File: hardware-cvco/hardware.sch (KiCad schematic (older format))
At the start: 2 parts, among them J1 Conn_Coaxial, Y1 CVCO55

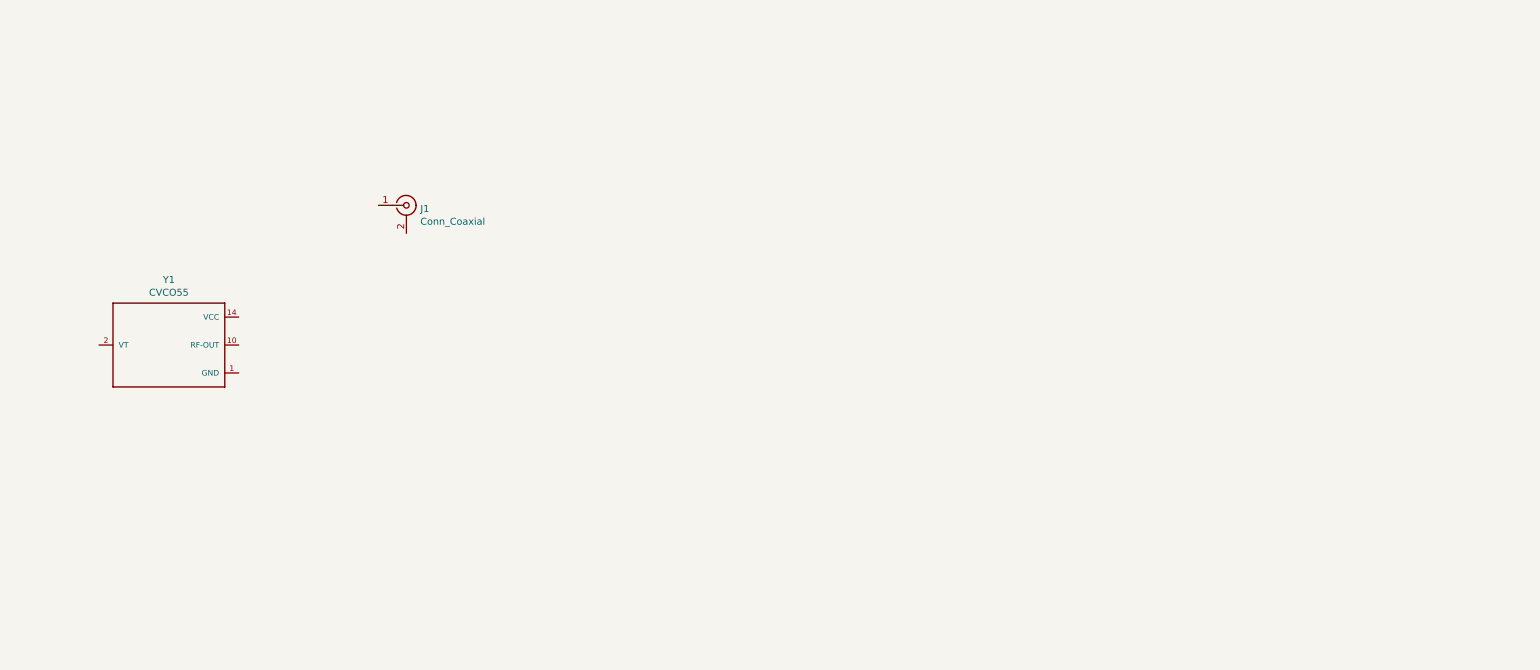
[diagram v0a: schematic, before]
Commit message: 500-1000 MHz & 1000-2000 MHz Crystek VCOs.
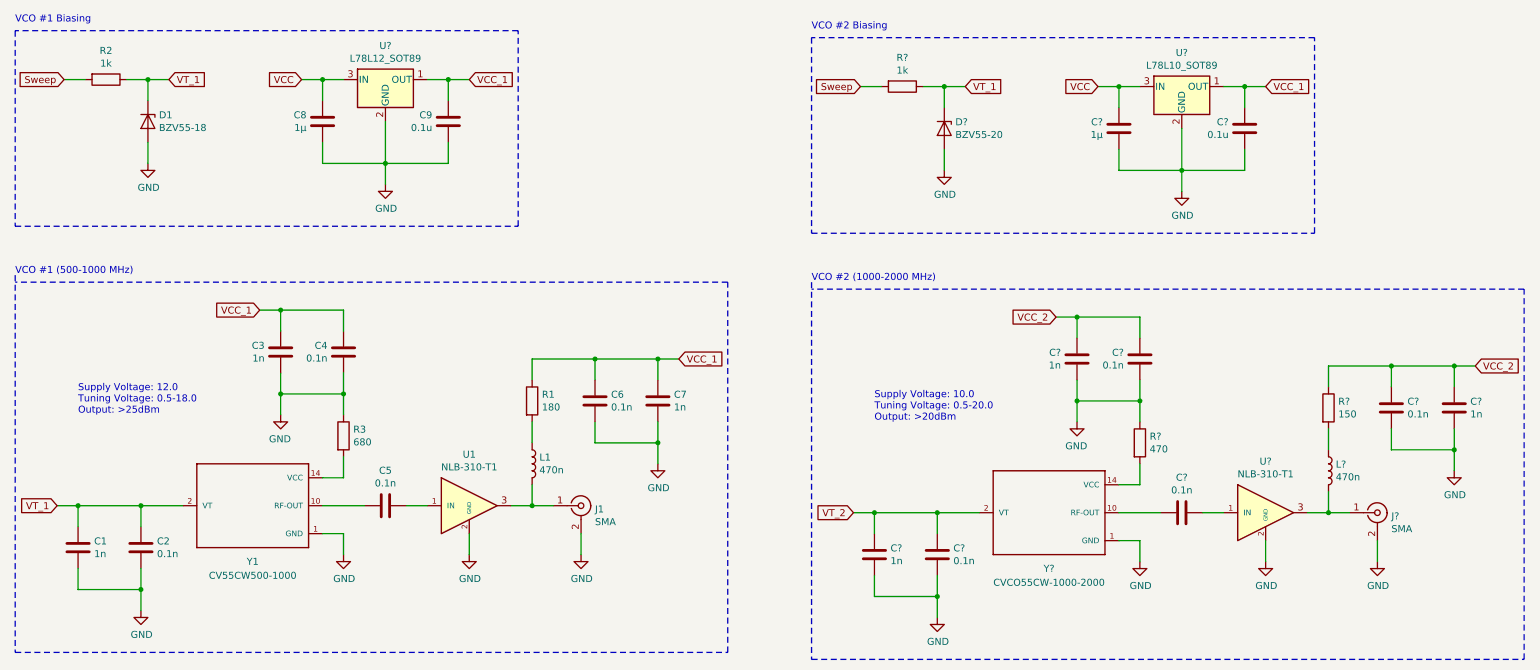
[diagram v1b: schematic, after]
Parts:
- added C1, C3, C7, C? (x3): 1n, symbol Device:C
- added C2, C4, C5, C6, C? (x4): 0.1n, symbol Device:C
- added C8, C?: 1μ, symbol Device:C
- added C9, C?: 0.1u, symbol Device:C
- added D1: BZV55-18, symbol Device:D_Zener
- added D?: BZV55-20, symbol Device:D_Zener
- added J?: SMA, Connector_Coaxial:SMA_Amphenol_132134_Vertical, symbol Connector:Conn_Coaxial
- added L1, L?: 470n, symbol Device:L
- added R1: 180, symbol Device:R
- added R2, R?: 1k, symbol Device:R
- added R3: 680, symbol Device:R
- added R?: 150, symbol Device:R
- added R?: 470, symbol Device:R
- added U1, U?: NLB-310-T1, CVCO:Micro-X-4, symbol CVCO:NLB-310
- added U?: L78L12_SOT89, Package_TO_SOT_SMD:SOT-89-3, symbol Regulator_Linear:L78L12_SOT89
- added U?: L78L10_SOT89, Package_TO_SOT_SMD:SOT-89-3, symbol Regulator_Linear:L78L10_SOT89
- added Y?: CVCO55CW-1000-2000, CVCO:CVCO55, symbol CVCO:CVCO55
- J1: value Conn_Coaxial -> SMA
- Y1: value CVCO55 -> CV55CW500-1000
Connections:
- net GND: now also J1.2 (Ext), C1.2, C2.2, C3.2, C4.2, C6.2, C7.2, C8.2, C9.2, C?.2, C?.2, C?.2, C?.2, C?.2, C?.2, C?.2, C?.2, D1.2 (A), D?.2 (A), J?.2 (Ext), R3.1, R?.1, U1.2 (GND), U1.4 (GND), U?.2 (GND), U?.2 (GND), U?.2 (GND), U?.4 (GND), Y?.1 (GND), Y?.11 (GND), Y?.12 (GND), Y?.13 (GND), Y?.15 (GND), Y?.16 (GND), Y?.3 (GND), Y?.4 (GND), Y?.5 (GND), Y?.6 (GND), Y?.7 (GND), Y?.8 (GND), Y?.9 (GND)
- net at J1.1 (In): now also L1.2, U1.3
- net at Y1.10 (RF-OUT): now also C5.2
- net at Y1.14 (VCC): now also R3.2
- net VT_1: now reaches Y1.2 (VT)
- net VT_1: now also C1.1, C2.1, D1.1 (K), D?.1 (K), R2.1, R?.1
- new net: J?.1 (In), L?.2, U?.3
- new net: C?.2, Y?.10 (RF-OUT)
- new net: R?.2, Y?.14 (VCC)
- new net: C?.1, U?.1 (IN)
- new net: L?.1, R?.2
- new net: C5.1, U1.1 (IN)
- new net: L1.1, R1.2
- new net Sweep: R2.2, R?.2
- new net VCC: C8.1, C?.1, U?.3 (IN), U?.3 (IN)
- new net VCC_1: C3.1, C4.1, C6.1, C7.1, C9.1, C?.1, R1.1, U?.1 (OUT), U?.1 (OUT)
- new net VCC_2: C?.1, C?.1, C?.1, C?.1, R?.1
- new net VT_2: C?.1, C?.1, Y?.2 (VT)
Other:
- note added: "Supply Voltage: 10.0\nTuning Voltage: 0.5-20.0\nOutput: >20dBm"
- note added: "Supply Voltage: 12.0\nTuning Voltage: 0.5-18.0\nOutput: >25dBm"
- note added: "VCO #1 (500-1000 MHz)"
- note added: "VCO #1 Biasing"
- note added: "VCO #2 (1000-2000 MHz)"
- note added: "VCO #2 Biasing"
- moved on the sheet: J1, Y1

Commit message: 1600-3200 MHz & 3180-3710 MHz Crystek VCOs.
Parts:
- added BT1: 3.7V, Connector_Wire:SolderWirePad_1x02_P3.81mm_Drill0.8mm, symbol Device:Battery_Cell
- added C12, C7: 10μF, Capacitor_SMD:C_0603_1608Metric_Pad1.05x0.95mm_HandSolder, symbol Device:C
- added C15, C9: 0.1μF, Capacitor_SMD:C_0603_1608Metric_Pad1.05x0.95mm_HandSolder, symbol Device:C
- added C8: 1μF, Capacitor_SMD:C_0603_1608Metric_Pad1.05x0.95mm_HandSolder, symbol Device:CP
- added C? (x6): 1n, symbol Device:C
- added C? (x6): 0.1n, symbol Device:C
- added C?: 33pF, symbol Device:C
- added C? (x2): 0.1u, symbol Device:C
- added C? (x2): 1μ, symbol Device:C
- added C?: 27pF, symbol Device:C
- added D3: GHC-YR, LED_SMD:LED_0603_1608Metric_Pad1.05x0.95mm_HandSolder, symbol Device:LED
- added D4: BHC-ZL, LED_SMD:LED_0603_1608Metric_Pad1.05x0.95mm_HandSolder, symbol Device:LED
- added D?: BZV55-20, symbol Device:D_Zener
- added D?: BZV55-16, symbol Device:D_Zener
- added J? (x2): SMA, Connector_Coaxial:SMA_Amphenol_132134_Vertical, symbol Connector:Conn_Coaxial
- added L? (x2): 470n, symbol Device:L
- added R10: 2k, Resistor_SMD:R_0603_1608Metric_Pad1.05x0.95mm_HandSolder, symbol Device:R
- added R17: 100, Resistor_SMD:R_0603_1608Metric_Pad1.05x0.95mm_HandSolder, symbol Device:R
- added R19: 1k, Resistor_SMD:R_0603_1608Metric_Pad1.05x0.95mm_HandSolder, symbol Device:R
- added R4, R5: 68, Resistor_SMD:R_0603_1608Metric_Pad1.05x0.95mm_HandSolder, symbol Device:R
- added R6: 180, Resistor_SMD:R_0603_1608Metric_Pad1.05x0.95mm_HandSolder, symbol Device:R
- added R?: 82, symbol Device:R
- added R? (x2): 1k, symbol Device:R
- added R?: 220, symbol Device:R
- added R?: 120, symbol Device:R
- added R?: 270, symbol Device:R
- added U3: TP4056, Package_SO:SSOP-8_2.95x2.8mm_P0.65mm, symbol Missing:TP4056
- added U4: DW01+G, Package_TO_SOT_SMD:SOT-23-6_Handsoldering, symbol Missing:DW01
- added U5: FS8205, Package_TO_SOT_SMD:SOT-23-6_Handsoldering, symbol Missing:FS8205
- added U? (x2): NLB-310-T1, CVCO:Micro-X-4, symbol CVCO:NLB-310
- added U?: L78L05_SOT89, Package_TO_SOT_SMD:SOT-89-3, symbol Regulator_Linear:L78L05_SOT89
- added U?: L78L08_SOT89, Package_TO_SOT_SMD:SOT-89-3, symbol Regulator_Linear:L78L08_SOT89
- added U? (x3): LM358, symbol Amplifier_Operational:LM358
- added U?: LM317_3PinPackage, symbol Regulator_Linear:LM317_3PinPackage
- added U?: MC34063AD, Package_SO:SOIC-8_3.9x4.9mm_P1.27mm, symbol Regulator_Switching:MC34063AD
- added Y?: CV55BE1600-3200, CVCO:CVCO55, symbol CVCO:CVCO55
- added Y?: CVCO55CC-3180-3710, CVCO:CVCO55, symbol CVCO:CVCO55
- C5: value 0.1n -> 100pF
- C?: value 0.1n -> 47pF
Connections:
- net labels added: BAT+, BAT-, BP_CS, BP_OC, BP_OD, BP_VDD, BP_VSS, LM_VDD, VCC_3, VCC_4, VT_3, VT_4
- wire segments 114 -> 294
- no-connect marks 0 -> 3
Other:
- note added: "580mA Battery Management"
- note added: "Battery Protection"
- note added: "Supply Voltage: 5.0\nTuning Voltage: 0.5-20.0\nOutput: >20dBm"
- note added: "Supply Voltage: 8.0\nTuning Voltage: 0.5-16.0\nOutput: >15dBm"
- note added: "VCO #3 (1600-3200 MHz)"
- note added: "VCO #3 Biasing"
- note added: "VCO #4 (3180-3710 MHz)"
- note added: "VCO #4 Biasing"
- moved on the sheet: C1, C2, C3, C4, C5, C6, C7, C8, C9, C?, D1, D?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

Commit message: Additional VCOs for 100-500 MHz range.
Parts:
- added C1, C17, C19, C23, C35, C38, C42, C5, C54: 1n, symbol Device:C
- added C11: 470pF, symbol Device:C
- added C13, C31, C50: 0.1u, symbol Device:C
- added C15, C21, C27, C3, C33, C40, C46, C52, C9: 0.1n, symbol Device:C
- added C25, C44, C7: 1μ, symbol Device:C
- added C29: 220pF, symbol Device:C
- added C48: 22pF, symbol Device:C
- added D1: BZV55-5, symbol Device:D_Zener
- added D3: BZV55-18, symbol Device:D_Zener
- added D6: BZV55-20, symbol Device:D_Zener
- added J1, J3, J6: SMA, Connector_Coaxial:SMA_Amphenol_132134_Vertical, symbol Connector:Conn_Coaxial
- added L1, L3, L6: 470n, symbol Device:L
- added R1, R14, R7: 1k, symbol Device:R
- added R11: 180, symbol Device:R
- added R16: 470, symbol Device:R
- added R18: 150, symbol Device:R
- added R3: 220, symbol Device:R
- added R5: 82, symbol Device:R
- added R9: 560, symbol Device:R
- added U10, U15, U4: NLB-310-T1, CVCO:Micro-X-4, symbol CVCO:NLB-310
- added U13: L78L08_SOT89, Package_TO_SOT_SMD:SOT-89-3, symbol Regulator_Linear:L78L08_SOT89
- added U2: L78L05_SOT89, Package_TO_SOT_SMD:SOT-89-3, symbol Regulator_Linear:L78L05_SOT89
- added U8: L78L12_SOT89, Package_TO_SOT_SMD:SOT-89-3, symbol Regulator_Linear:L78L12_SOT89
- added Y1: CVCO55CW-0100-0200, CVCO:CVCO55, symbol CVCO:CVCO55
- added Y3: CVCO55CW-0200-0500, CVCO:CVCO55, symbol CVCO:CVCO55
- added Y6: CVCO55CW-3500-4500, CVCO:CVCO55, symbol CVCO:CVCO55
- gave numbers to parts that had none: 58
- renumbered C1 to C37, C2 to C39, C3 to C41, C8 to C43, C4 to C45, C5 to C47, C9 to C49, C6 to C51, C7 to C53, C7 to C56, C8 to C58, C9 to C59, C15 to C61, C12 to C66, D1 to D5, D3 to D8, D4 to D9, J1 to J5, L1 to L5, R2 to R13, R3 to R15, R1 to R17, R4 to R20, R17 to R21, R5 to R22, R6 to R23, R10 to R25, R19 to R26, U1 to U14, U4 to U16, U3 to U18, U5 to U19, Y1 to Y5
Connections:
- net labels added: VCC_5, VCC_6, VT_5, VT_6
- wire segments 294 -> 465
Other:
- note added: "Supply Voltage: 10.0\nTuning Voltage: 1.0-20.0\nOutput: >25dBm"
- note added: "Supply Voltage: 5\nTuning Voltage: 0.0-5.0\nOutput: >25dBm"
- note added: "VCO #1 (100-200 MHz)"
- note added: "VCO #2 (200-500 MHz)"
- note added: "VCO #3 (500-1000 MHz)"
- note added: "VCO #4 (1000-2000 MHz)"
- note added: "VCO #5 (1600-3200 MHz)"
- note added: "VCO #5 Biasing"
- note added: "VCO #6 (3180-3710 MHz)"
- note added: "VCO #6 Biasing"
- note added: "VCO #7 (3500-4500 MHz)"
- note added: "VCO #7 Biasing"
- note removed: "VCO #1 (500-1000 MHz)"
- note removed: "VCO #2 (1000-2000 MHz)"
- note removed: "VCO #3 (1600-3200 MHz)"
- note removed: "VCO #4 (3180-3710 MHz)"
- moved on the sheet: BT1, C10, C12, C14, C16, C18, C2, C20, C22, C24, C26, C28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

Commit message: Assigned footprints & part IDs.
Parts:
- removed BT1: 3.7V, Connector_Wire:SolderWirePad_1x02_P3.81mm_Drill0.8mm, symbol Device:Battery_Cell
- removed C58: 1μF, Capacitor_SMD:C_0603_1608Metric_Pad1.05x0.95mm_HandSolder, symbol Device:CP
- removed C60, C68: 1n, symbol Device:C
- removed C65: 0.1u, symbol Device:C
- removed C66: 10μF, Capacitor_SMD:C_0603_1608Metric_Pad1.05x0.95mm_HandSolder, symbol Device:C
- removed C67: 0.1n, symbol Device:C
- removed D8: GHC-YR, LED_SMD:LED_0603_1608Metric_Pad1.05x0.95mm_HandSolder, symbol Device:LED
- removed D9: BHC-ZL, LED_SMD:LED_0603_1608Metric_Pad1.05x0.95mm_HandSolder, symbol Device:LED
- removed R20, R22: 68, Resistor_SMD:R_0603_1608Metric_Pad1.05x0.95mm_HandSolder, symbol Device:R
- removed R21: 100, Resistor_SMD:R_0603_1608Metric_Pad1.05x0.95mm_HandSolder, symbol Device:R
- removed R23: 180, Resistor_SMD:R_0603_1608Metric_Pad1.05x0.95mm_HandSolder, symbol Device:R
- removed R25: 2k, Resistor_SMD:R_0603_1608Metric_Pad1.05x0.95mm_HandSolder, symbol Device:R
- removed R26: 1k, Resistor_SMD:R_0603_1608Metric_Pad1.05x0.95mm_HandSolder, symbol Device:R
- removed U1: LM317_3PinPackage, symbol Regulator_Linear:LM317_3PinPackage
- removed U12: L78L12_SOT89, Package_TO_SOT_SMD:SOT-89-3, symbol Regulator_Linear:L78L12_SOT89
- removed U13: L78L08_SOT89, Package_TO_SOT_SMD:SOT-89-3, symbol Regulator_Linear:L78L08_SOT89
- removed U16: DW01+G, Package_TO_SOT_SMD:SOT-23-6_Handsoldering, symbol Missing:DW01
- removed U18: TP4056, Package_SO:SSOP-8_2.95x2.8mm_P0.65mm, symbol Missing:TP4056
- removed U19: FS8205, Package_TO_SOT_SMD:SOT-23-6_Handsoldering, symbol Missing:FS8205
- removed U3: L78L05_SOT89, Package_TO_SOT_SMD:SOT-89-3, symbol Regulator_Linear:L78L05_SOT89
- removed U6: MC34063AD, Package_SO:SOIC-8_3.9x4.9mm_P1.27mm, symbol Regulator_Switching:MC34063AD
- removed U7: LM358, symbol Amplifier_Operational:LM358
- added C58: 1μ, Capacitor_SMD:C_0805_2012Metric_Pad1.15x1.40mm_HandSolder, symbol Device:C
- added U11: L78L12_SOT89, Package_TO_SOT_SMD:SOT-89-3, symbol Regulator_Linear:L78L12_SOT89
- added U12: L78L10_SOT89, Package_TO_SOT_SMD:SOT-89-3, symbol Regulator_Linear:L78L10_SOT89
- added U2: L78L05_SOT89, Package_TO_SOT_SMD:SOT-89-3, symbol Regulator_Linear:L78L05_SOT89
- C1, C10, C15, C16, C17, C18, C19, C2, C20, C21, C22, C23, C24, C27, C28, C3, C33, C34, C35, C36, C37, C38, C39, C4, C40, C41, C42, C45, C46, C5, C51, C52, C53, C54, C55, C6, C9: footprint (none) -> Capacitor_SMD:C_0805_2012Metric_Pad1.15x1.40mm_HandSolder; LCSC Part # (none) -> 0805
- C11: footprint (none) -> Capacitor_SMD:C_0805_2012Metric_Pad1.15x1.40mm_HandSolder; LCSC Part # (none) -> C1743
- C12: footprint (none) -> Capacitor_SMD:C_0805_2012Metric_Pad1.15x1.40mm_HandSolder; LCSC Part # (none) -> C157687
- C13, C14, C31, C32, C49, C50: footprint (none) -> Capacitor_SMD:C_0805_2012Metric_Pad1.15x1.40mm_HandSolder; LCSC Part # (none) -> C495959
- C25, C26, C43, C44, C7, C8: footprint (none) -> Capacitor_SMD:C_0805_2012Metric_Pad1.15x1.40mm_HandSolder; LCSC Part # (none) -> C111768
- C29: footprint (none) -> Capacitor_SMD:C_0805_2012Metric_Pad1.15x1.40mm_HandSolder; LCSC Part # (none) -> C1727
- C30: footprint (none) -> Capacitor_SMD:C_0805_2012Metric_Pad1.15x1.40mm_HandSolder; LCSC Part # (none) -> C8031
- C47: footprint (none) -> Capacitor_SMD:C_0805_2012Metric_Pad1.15x1.40mm_HandSolder; LCSC Part # (none) -> C1790
- C48: footprint (none) -> Capacitor_SMD:C_0805_2012Metric_Pad1.15x1.40mm_HandSolder; LCSC Part # (none) -> C24658
- C56: value 10μF -> 0.1n; footprint Capacitor_SMD:C_0603_1608Metric_Pad1.05x0.95mm_HandSolder -> Capacitor_SMD:C_0805_2012Metric_Pad1.15x1.40mm_HandSolder; LCSC Part # (none) -> 0805
- C57, C63: value 0.1n -> 1n; footprint (none) -> Capacitor_SMD:C_0805_2012Metric_Pad1.15x1.40mm_HandSolder; LCSC Part # (none) -> 0805
- C59: value 0.1μF -> 0.1n; footprint Capacitor_SMD:C_0603_1608Metric_Pad1.05x0.95mm_HandSolder -> Capacitor_SMD:C_0805_2012Metric_Pad1.15x1.40mm_HandSolder; LCSC Part # (none) -> 0805
- C60: renamed from C64; footprint (none) -> Capacitor_SMD:C_0805_2012Metric_Pad1.15x1.40mm_HandSolder; LCSC Part # (none) -> C107118
- C61: value 0.1μF -> 0.1u; footprint Capacitor_SMD:C_0603_1608Metric_Pad1.05x0.95mm_HandSolder -> Capacitor_SMD:C_0805_2012Metric_Pad1.15x1.40mm_HandSolder; LCSC Part # (none) -> C495959
- C62: value 1μ -> 0.1n; footprint (none) -> Capacitor_SMD:C_0805_2012Metric_Pad1.15x1.40mm_HandSolder; LCSC Part # (none) -> 0805
- D1: value BZV55-5 -> 5V; footprint (none) -> Package_TO_SOT_SMD:SOT-23; LCSC Part # (none) -> C455057
- D2, D6, D7: value BZV55-20 -> 20V; footprint (none) -> Package_TO_SOT_SMD:SOT-23; LCSC Part # (none) -> C118582
- D3, D5: value BZV55-18 -> 18V; footprint (none) -> Package_TO_SOT_SMD:SOT-23; LCSC Part # (none) -> C85086
- D4: value BZV55-16 -> 16V; footprint (none) -> Package_TO_SOT_SMD:SOT-23; LCSC Part # (none) -> C44457
- J1, J2, J3, J4: LCSC Part # (none) -> C530661
- J6: renamed from J5; LCSC Part # (none) -> C530661
- J7: renamed from J6; LCSC Part # (none) -> C530661
- J8: renamed from J7; LCSC Part # (none) -> C530661
- L1, L2, L3, L4, L5, L6, L7: footprint (none) -> Inductor_SMD:L_0805_2012Metric_Pad1.15x1.40mm_HandSolder; LCSC Part # (none) -> C393986
- R1, R13, R14, R19, R2, R8: footprint (none) -> Resistor_SMD:R_0805_2012Metric_Pad1.15x1.40mm_HandSolder; LCSC Part # (none) -> C17513
- R10: footprint (none) -> Resistor_SMD:R_0805_2012Metric_Pad1.15x1.40mm_HandSolder; LCSC Part # (none) -> C115004
- R11, R17: footprint (none) -> Resistor_SMD:R_0805_2012Metric_Pad1.15x1.40mm_HandSolder; LCSC Part # (none) -> C104048
- R12: footprint (none) -> Resistor_SMD:R_0805_2012Metric_Pad1.15x1.40mm_HandSolder; LCSC Part # (none) -> C114244
- R15: footprint (none) -> Resistor_SMD:R_0805_2012Metric_Pad1.15x1.40mm_HandSolder; LCSC Part # (none) -> C17798
- R16: footprint (none) -> Resistor_SMD:R_0805_2012Metric_Pad1.15x1.40mm_HandSolder; LCSC Part # (none) -> C114564
- R18: footprint (none) -> Resistor_SMD:R_0805_2012Metric_Pad1.15x1.40mm_HandSolder; LCSC Part # (none) -> C25283
- R20: renamed from R24; footprint (none) -> Resistor_SMD:R_0805_2012Metric_Pad1.15x1.40mm_HandSolder; LCSC Part # (none) -> C114564
- R21: renamed from R27; footprint (none) -> Resistor_SMD:R_0805_2012Metric_Pad1.15x1.40mm_HandSolder; LCSC Part # (none) -> C25283
- R3, R4: footprint (none) -> Resistor_SMD:R_0805_2012Metric_Pad1.15x1.40mm_HandSolder; LCSC Part # (none) -> C165202
- R5, R6: footprint (none) -> Resistor_SMD:R_0805_2012Metric_Pad1.15x1.40mm_HandSolder; LCSC Part # (none) -> C25329
- R7: footprint (none) -> Resistor_SMD:R_0805_2012Metric_Pad1.15x1.40mm_HandSolder
- R9: footprint (none) -> Resistor_SMD:R_0805_2012Metric_Pad1.15x1.40mm_HandSolder; LCSC Part # (none) -> C28636
- U1: renamed from U2; LCSC Part # (none) -> C156436
- U13: renamed from U14; Mouser Part # (none) -> 772-NLB-310
- U14: renamed from U15; Mouser Part # (none) -> 772-NLB-310
- U16: renamed from U17; LCSC Part # (none) -> C122848
- U17: renamed from U20; Mouser Part # (none) -> 772-NLB-310
- U3: renamed from U4; Mouser Part # (none) -> 772-NLB-310
- U4: renamed from U5; Mouser Part # (none) -> 772-NLB-310
- U6: renamed from U8; LCSC Part # (none) -> C351431
- U7: renamed from U9; LCSC Part # (none) -> C351430
- U8: renamed from U10; Mouser Part # (none) -> 772-NLB-310
- U9: renamed from U11; Mouser Part # (none) -> 772-NLB-310
- Y1: Mouser Part # (none) -> 549-CV55CW0100-0200
- Y2, Y7: Mouser Part # (none) -> 549-CV55CW1000-2000
- Y3: Mouser Part # (none) -> 549-CV55CW0200-0500
- Y4: Mouser Part # (none) -> 549-CVCO55CC31803710
- Y5: value CV55CW500-1000 -> CV55CW500-1000; Mouser Part # (none) -> 549-CV55CW500-1000
- Y6: Mouser Part # (none) -> 549-CVC55CW3500-4500
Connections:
- net labels removed: BAT+, BAT-, BP_CS, BP_OC, BP_OD, BP_VDD, BP_VSS, LM_VDD
- wire segments 465 -> 399
- no-connect marks 3 -> 0
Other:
- note removed: "580mA Battery Management"
- note removed: "Battery Protection"

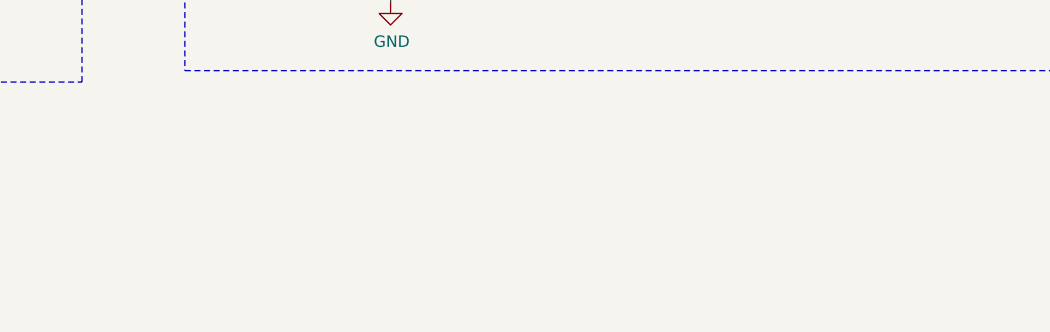
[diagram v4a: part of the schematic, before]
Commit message: Added CVCO datasheets.
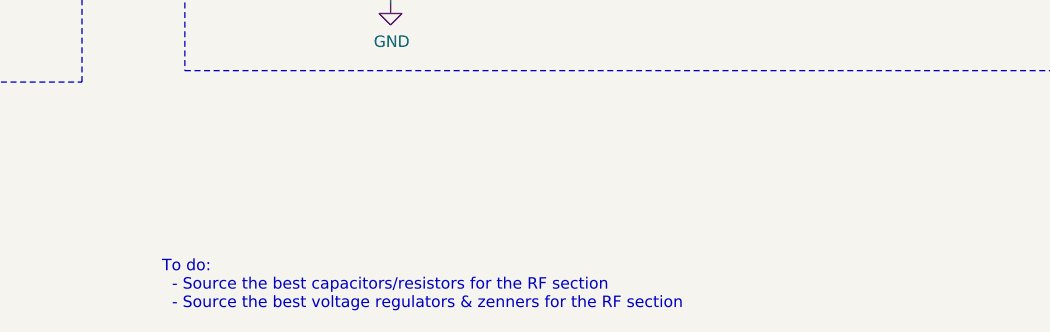
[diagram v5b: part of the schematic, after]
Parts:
- Y2: Mouser Part # 549-CV55CW1000-2000 -> 549-CV55BE1600-3200
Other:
- note added: "To do:\n - Source the best capacitors/resistors for the RF section\n - Source the best voltage regulators & zenners for the RF section"
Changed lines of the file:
@@
 F 1 "CV55CW500-1000" H 13600 3950 50  0000 C CNN
 F 2 "CVCO:CVCO55" H 13069 3978 50  0001 L BNN
-F 3 "None" H 13600 4450 50  0001 L BNN
+F 3 "https://www.crystek.com/microwave/admin/webapps/welcome/files/vco/CVCO55CW-0500-1000.pdf" H 13600 4450 50  0001 L BNN
 F 4 "549-CV55CW500-1000" H 13600 4450 50  0001 C CNN "Mouser Part #"
 	1    13600 4450
@@
 F 1 "CVCO55CW-1000-2000" H 19100 3950 50  0000 C CNN
 F 2 "CVCO:CVCO55" H 18569 3978 50  0001 L BNN
-F 3 "None" H 19100 4450 50  0001 L BNN
+F 3 "https://www.crystek.com/microwave/admin/webapps/welcome/files/vco/CVCO55CW-1000-2000.pdf" H 19100 4450 50  0001 L BNN
 F 4 "549-CV55CW1000-2000" H 19100 4450 50  0001 C CNN "Mouser Part #"
 	1    19100 4450
@@
 F 1 "CV55BE1600-3200" H 2600 9000 50  0000 C CNN
 F 2 "CVCO:CVCO55" H 2069 9028 50  0001 L BNN
-F 3 "None" H 2600 9500 50  0001 L BNN
-F 4 "549-CV55CW1000-2000" H 2600 9500 50  0001 C CNN "Mouser Part #"
+F 3 "https://www.crystek.com/microwave/admin/webapps/welcome/files/vco/CVCO55CW-1600-3200.pdf" H 2600 9500 50  0001 L BNN
+F 4 "549-CV55BE1600-3200" H 2600 9500 50  0001 C CNN "Mouser Part #"
 	1    2600 9500
 	1    0    0    -1
@@
 F 1 "CVCO55CC-3180-3710" H 8100 9000 50  0000 C CNN
 F 2 "CVCO:CVCO55" H 7569 9028 50  0001 L BNN
-F 3 "None" H 8100 9500 50  0001 L BNN
+F 3 "https://www.crystek.com/microwave/admin/webapps/welcome/files/vco/CVCO55CC-3180-3710.pdf" H 8100 9500 50  0001 L BNN
 F 4 "549-CVCO55CC31803710" H 8100 9500 50  0001 C CNN "Mouser Part #"
 	1    8100 9500
@@
 F 1 "CVCO55CW-0100-0200" H 2600 3950 50  0000 C CNN
 F 2 "CVCO:CVCO55" H 2069 3978 50  0001 L BNN
-F 3 "None" H 2600 4450 50  0001 L BNN
+F 3 "https://www.crystek.com/microwave/admin/webapps/welcome/files/vco/CVCO55CW-0100-0200.pdf" H 2600 4450 50  0001 L BNN
 F 4 "549-CV55CW0100-0200" H 2600 4450 50  0001 C CNN "Mouser Part #"
 	1    2600 4450
@@
 F 1 "CVCO55CW-0200-0500" H 8100 3950 50  0000 C CNN
 F 2 "CVCO:CVCO55" H 7569 3978 50  0001 L BNN
-F 3 "None" H 8100 4450 50  0001 L BNN
+F 3 "https://www.crystek.com/microwave/admin/webapps/welcome/files/vco/CVCO55CW-0200-0500.pdf" H 8100 4450 50  0001 L BNN
 F 4 "549-CV55CW0200-0500" H 8100 4450 50  0001 C CNN "Mouser Part #"
 	1    8100 4450
@@
 F 1 "CVCO55CW-3500-4500" H 13650 8950 50  0000 C CNN
 F 2 "CVCO:CVCO55" H 13119 8978 50  0001 L BNN
-F 3 "None" H 13650 9450 50  0001 L BNN
+F 3 "https://www.crystek.com/microwave/admin/webapps/welcome/files/vco/CVCO55CW-3500-4500.pdf" H 13650 9450 50  0001 L BNN
 F 4 "549-CVC55CW3500-4500" H 13650 9450 50  0001 C CNN "Mouser Part #"
 	1    13650 9450
@@
 	1    0    0    -1
 $EndComp
+Text Notes 11850 11550 0    50   ~ 0
+To do:\n  - Source the best capacitors/resistors for the RF section\n  - Source the best voltage regulators & zenners for the RF section
 $EndSCHEMATC
